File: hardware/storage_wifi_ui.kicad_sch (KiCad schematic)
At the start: 28 parts, among them J16 Keyboard KIN0-7 / KOUT0-7, J17 Keyboard power/reference, J18 I2C0, J19 Full-size SD, SPI, J20 ESP-01/ESP-01S socket, SW2 ESP_PROG, U34 AMS1117-3.3

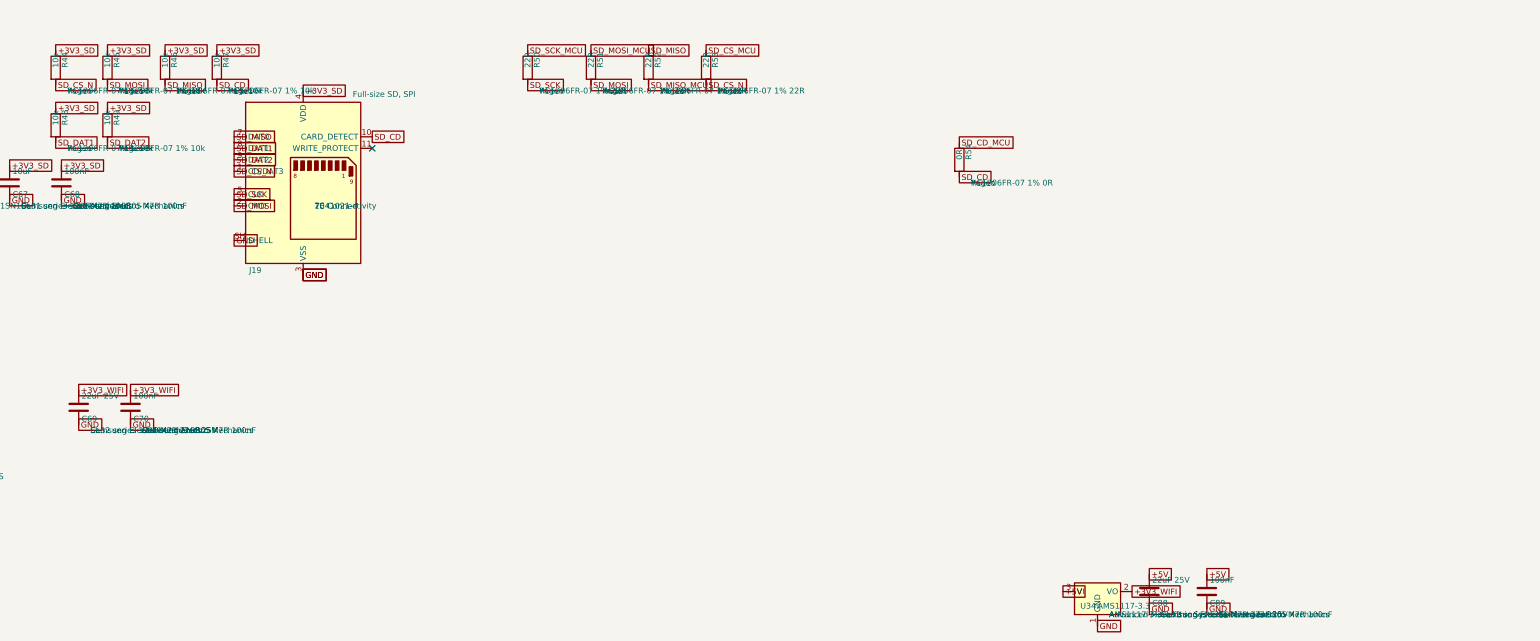
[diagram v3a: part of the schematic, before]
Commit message: Standardize passives and add microSD alternate
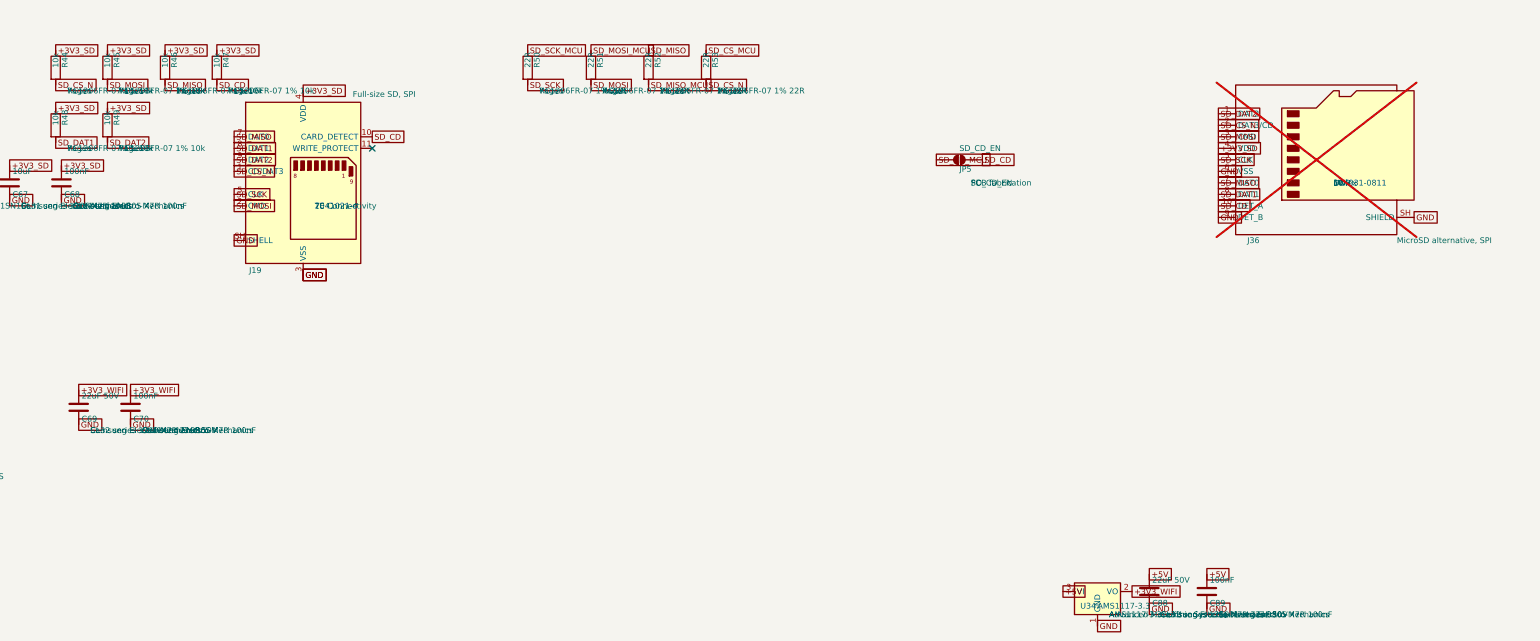
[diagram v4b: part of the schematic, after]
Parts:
- removed R54: 0R, Resistor_SMD:R_1206_3216Metric, symbol Device:R
- added J36: MicroSD alternative, SPI, Connector_Card:microSD_HC_Molex_104031-0811, symbol Connector:Micro_SD_Card_Det2
- added JP5: SD_CD_EN, LeanCam:SolderJumper_2_Open_1206Gap, symbol Jumper:SolderJumper_2_Open
- C69, C88: value 22uF 25V -> 22uF 50V; MPN CL32 series 1210 X7R 22uF 25V -> CL32 series 1210 X7R 22uF 50V
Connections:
- net +3V3_SD: now also J36.4 (VDD)
- net GND: now also J36.6 (VSS), J36.9 (DET_B), J36.SH (SHIELD)
- net SD_CD: now also J36.10 (DET_A), JP5.2 (B)
- net SD_CD_MCU: now also JP5.1 (A)
- net SD_CS_N: now also J36.2 (DAT3/CD)
- net SD_DAT1: now also J36.8 (DAT1)
- net SD_DAT2: now also J36.1 (DAT2)
- net SD_MISO: now also J36.7 (DAT0)
- net SD_MOSI: now also J36.3 (CMD)
- net SD_SCK: now also J36.5 (CLK)

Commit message: BOM simplification
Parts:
- C67: value 10uF -> 10uF 25V; MPN CL31 series 1206 X7R 10uF -> CL31 series 1206 X7R 10uF 25V
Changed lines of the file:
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@@
 		(instances
 			(project "Storage, Wi-Fi and UI"
-				(path "/9f4f8ddb-6d75-424f-85af-50d3b0c33d12"
+				(path "/ebd1e8ca-9dff-4053-89c8-43c30a776960"
 					(reference "J16")
 					(unit 1)
@@
 		(instances
 			(project "Storage, Wi-Fi and UI"
-				(path "/9f4f8ddb-6d75-424f-85af-50d3b0c33d12"
+				(path "/ebd1e8ca-9dff-4053-89c8-43c30a776960"
 					(reference "J17")
 					(unit 1)
@@
 		(instances
 			(project "Storage, Wi-Fi and UI"
-				(path "/9f4f8ddb-6d75-424f-85af-50d3b0c33d12"
+				(path "/ebd1e8ca-9dff-4053-89c8-43c30a776960"
 					(reference "RN22")
 					(unit 1)
@@
 		(instances
 			(project "Storage, Wi-Fi and UI"
-				(path "/9f4f8ddb-6d75-424f-85af-50d3b0c33d12"
+				(path "/ebd1e8ca-9dff-4053-89c8-43c30a776960"
 					(reference "RN24")
 					(unit 1)
@@
 		(instances
 			(project "Storage, Wi-Fi and UI"
-				(path "/9f4f8ddb-6d75-424f-85af-50d3b0c33d12"
+				(path "/ebd1e8ca-9dff-4053-89c8-43c30a776960"
 					(reference "J18")
 					(unit 1)
@@
 		(instances
 			(project "Storage, Wi-Fi and UI"
-				(path "/9f4f8ddb-6d75-424f-85af-50d3b0c33d12"
+				(path "/ebd1e8ca-9dff-4053-89c8-43c30a776960"
 					(reference "J19")
 					(unit 1)
@@
 		(instances
 			(project "Storage, Wi-Fi and UI"
-				(path "/9f4f8ddb-6d75-424f-85af-50d3b0c33d12"
+				(path "/ebd1e8ca-9dff-4053-89c8-43c30a776960"
 					(reference "R44")
 					(unit 1)
@@
 		(instances
 			(project "Storage, Wi-Fi and UI"
-				(path "/9f4f8ddb-6d75-424f-85af-50d3b0c33d12"
+				(path "/ebd1e8ca-9dff-4053-89c8-43c30a776960"
 					(reference "R45")
 					(unit 1)
@@
 		(instances
 			(project "Storage, Wi-Fi and UI"
-				(path "/9f4f8ddb-6d75-424f-85af-50d3b0c33d12"
+				(path "/ebd1e8ca-9dff-4053-89c8-43c30a776960"
 					(reference "R46")
 					(unit 1)
@@
 		(instances
 			(project "Storage, Wi-Fi and UI"
-				(path "/9f4f8ddb-6d75-424f-85af-50d3b0c33d12"
+				(path "/ebd1e8ca-9dff-4053-89c8-43c30a776960"
 					(reference "R47")
 					(unit 1)
@@
 		(instances
 			(project "Storage, Wi-Fi and UI"
-				(path "/9f4f8ddb-6d75-424f-85af-50d3b0c33d12"
+				(path "/ebd1e8ca-9dff-4053-89c8-43c30a776960"
 					(reference "R48")
 					(unit 1)
@@
 		(instances
 			(project "Storage, Wi-Fi and UI"
-				(path "/9f4f8ddb-6d75-424f-85af-50d3b0c33d12"
+				(path "/ebd1e8ca-9dff-4053-89c8-43c30a776960"
 					(reference "R49")
 					(unit 1)
@@
 		(instances
 			(project "Storage, Wi-Fi and UI"
-				(path "/9f4f8ddb-6d75-424f-85af-50d3b0c33d12"
+				(path "/ebd1e8ca-9dff-4053-89c8-43c30a776960"
 					(reference "R50")
 					(unit 1)
@@
 		(instances
 			(project "Storage, Wi-Fi and UI"
-				(path "/9f4f8ddb-6d75-424f-85af-50d3b0c33d12"
+				(path "/ebd1e8ca-9dff-4053-89c8-43c30a776960"
 					(reference "R51")
 					(unit 1)
@@
 		(instances
 			(project "Storage, Wi-Fi and UI"
-				(path "/9f4f8ddb-6d75-424f-85af-50d3b0c33d12"
+				(path "/ebd1e8ca-9dff-4053-89c8-43c30a776960"
 					(reference "R52")
 					(unit 1)
@@
 		(instances
 			(project "Storage, Wi-Fi and UI"
-				(path "/9f4f8ddb-6d75-424f-85af-50d3b0c33d12"
+				(path "/ebd1e8ca-9dff-4053-89c8-43c30a776960"
 					(reference "R53")
 					(unit 1)
@@
 		(instances
 			(project "Storage, Wi-Fi and UI"
-				(path "/9f4f8ddb-6d75-424f-85af-50d3b0c33d12"
+				(path "/ebd1e8ca-9dff-4053-89c8-43c30a776960"
 					(reference "FB2")
 					(unit 1)
@@
 			)
 		)
-		(property "Value" "10uF"
+		(property "Value" "10uF 25V"
 			(at 90.805 167.64 0.0000)
 			(effects
@@
 			)
 		)
-		(property "MPN" "CL31 series 1206 X7R 10uF"
+		(property "MPN" "CL31 series 1206 X7R 10uF 25V"
 			(at 92.71 175.2599 0)
 			(effects
@@
 		(instances
 			(project "Storage, Wi-Fi and UI"
-				(path "/9f4f8ddb-6d75-424f-85af-50d3b0c33d12"
+				(path "/ebd1e8ca-9dff-4053-89c8-43c30a776960"
 					(reference "C67")
 					(unit 1)
@@
 		(instances
 			(project "Storage, Wi-Fi and UI"
-				(path "/9f4f8ddb-6d75-424f-85af-50d3b0c33d12"
+				(path "/ebd1e8ca-9dff-4053-89c8-43c30a776960"
 					(reference "C68")
 					(unit 1)
@@
 		(instances
 			(project "Storage, Wi-Fi and UI"
-				(path "/9f4f8ddb-6d75-424f-85af-50d3b0c33d12"
+				(path "/ebd1e8ca-9dff-4053-89c8-43c30a776960"
 					(reference "JP5")
 					(unit 1)
@@
 		(instances
 			(project "Storage, Wi-Fi and UI"
-				(path "/9f4f8ddb-6d75-424f-85af-50d3b0c33d12"
+				(path "/ebd1e8ca-9dff-4053-89c8-43c30a776960"
 					(reference "J20")
 					(unit 1)
@@
 		(instances
 			(project "Storage, Wi-Fi and UI"
-				(path "/9f4f8ddb-6d75-424f-85af-50d3b0c33d12"
+				(path "/ebd1e8ca-9dff-4053-89c8-43c30a776960"
 					(reference "SW2")
 					(unit 1)
@@
 		(instances
 			(project "Storage, Wi-Fi and UI"
-				(path "/9f4f8ddb-6d75-424f-85af-50d3b0c33d12"
+				(path "/ebd1e8ca-9dff-4053-89c8-43c30a776960"
 					(reference "C69")
 					(unit 1)
@@
 		(instances
 			(project "Storage, Wi-Fi and UI"
-				(path "/9f4f8ddb-6d75-424f-85af-50d3b0c33d12"
+				(path "/ebd1e8ca-9dff-4053-89c8-43c30a776960"
 					(reference "C70")
 					(unit 1)
@@
 		(instances
 			(project "Storage, Wi-Fi and UI"
-				(path "/9f4f8ddb-6d75-424f-85af-50d3b0c33d12"
+				(path "/ebd1e8ca-9dff-4053-89c8-43c30a776960"
 					(reference "U34")
 					(unit 1)
@@
 		(instances
 			(project "Storage, Wi-Fi and UI"
-				(path "/9f4f8ddb-6d75-424f-85af-50d3b0c33d12"
+				(path "/ebd1e8ca-9dff-4053-89c8-43c30a776960"
 					(reference "C88")
 					(unit 1)
@@
 		(instances
 			(project "Storage, Wi-Fi and UI"
-				(path "/9f4f8ddb-6d75-424f-85af-50d3b0c33d12"
+				(path "/ebd1e8ca-9dff-4053-89c8-43c30a776960"
 					(reference "C89")
 					(unit 1)
@@
 		(instances
 			(project "Storage, Wi-Fi and UI"
-				(path "/9f4f8ddb-6d75-424f-85af-50d3b0c33d12"
+				(path "/ebd1e8ca-9dff-4053-89c8-43c30a776960"
 					(reference "RN36")
 					(unit 1)
@@
 		(instances
 			(project "Storage, Wi-Fi and UI"
-				(path "/9f4f8ddb-6d75-424f-85af-50d3b0c33d12"
+				(path "/ebd1e8ca-9dff-4053-89c8-43c30a776960"
 					(reference "J36")
 					(unit 1)

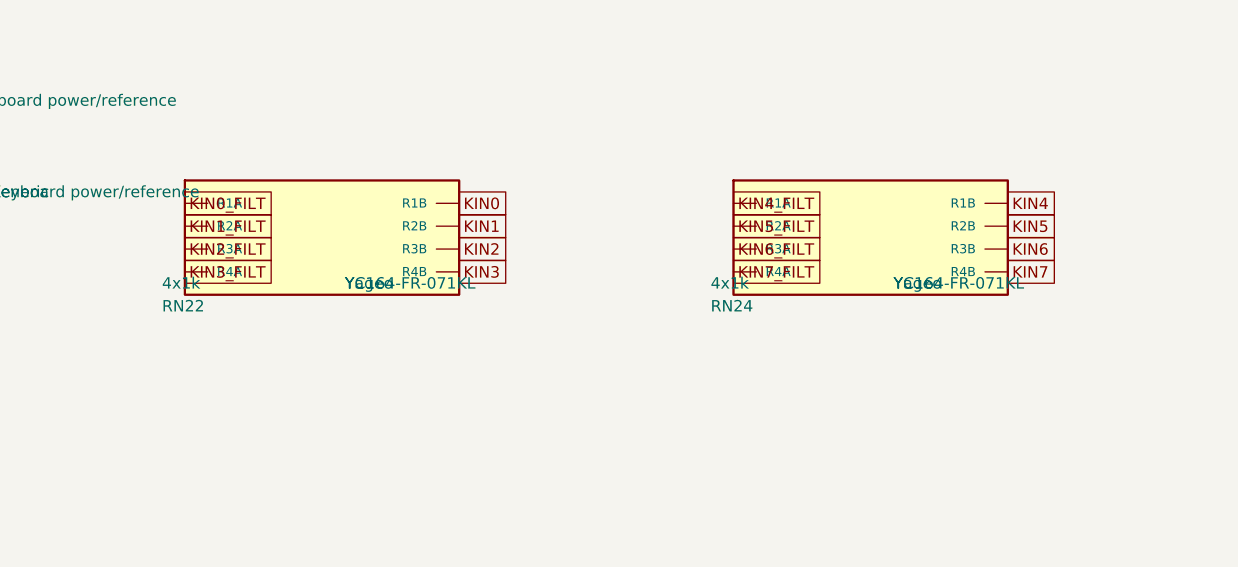
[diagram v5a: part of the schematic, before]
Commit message: Use 10k keyboard input networks
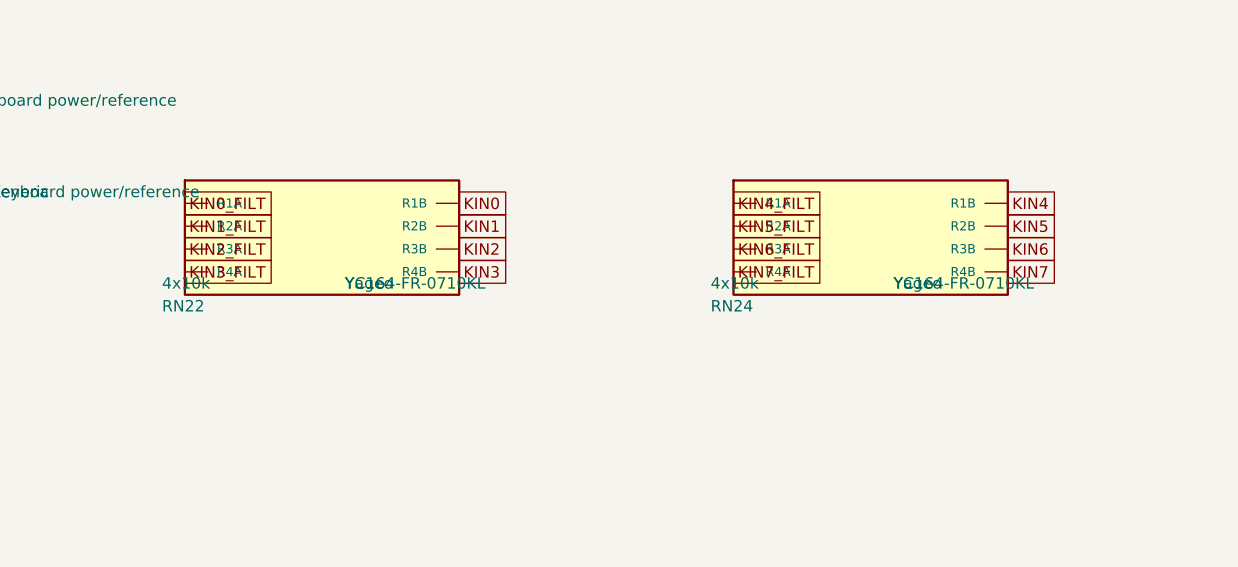
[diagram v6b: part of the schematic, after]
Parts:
- RN22, RN24: value 4x1k -> 4x10k; MPN YC164-FR-071KL -> YC164-FR-0710KL
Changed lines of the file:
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@@
 		(instances
 			(project "Storage, Wi-Fi and UI"
-				(path "/ebd1e8ca-9dff-4053-89c8-43c30a776960"
+				(path "/c5fb96bd-ffa6-4008-91b8-ee7edad8144e"
 					(reference "J16")
 					(unit 1)
@@
 		(instances
 			(project "Storage, Wi-Fi and UI"
-				(path "/ebd1e8ca-9dff-4053-89c8-43c30a776960"
+				(path "/c5fb96bd-ffa6-4008-91b8-ee7edad8144e"
 					(reference "J17")
 					(unit 1)
@@
 			)
 		)
-		(property "Value" "4x1k"
+		(property "Value" "4x10k"
 			(at 111.76 90.17 0.0000)
 			(effects
@@
 			)
 		)
-		(property "MPN" "YC164-FR-071KL"
+		(property "MPN" "YC164-FR-0710KL"
 			(at 132.08 90.1699 0)
 			(effects
@@
 		(instances
 			(project "Storage, Wi-Fi and UI"
-				(path "/ebd1e8ca-9dff-4053-89c8-43c30a776960"
+				(path "/c5fb96bd-ffa6-4008-91b8-ee7edad8144e"
 					(reference "RN22")
 					(unit 1)
@@
 			)
 		)
-		(property "Value" "4x1k"
+		(property "Value" "4x10k"
 			(at 172.72 90.17 0.0000)
 			(effects
@@
 			)
 		)
-		(property "MPN" "YC164-FR-071KL"
+		(property "MPN" "YC164-FR-0710KL"
 			(at 193.04 90.1699 0)
 			(effects
@@
 		(instances
 			(project "Storage, Wi-Fi and UI"
-				(path "/ebd1e8ca-9dff-4053-89c8-43c30a776960"
+				(path "/c5fb96bd-ffa6-4008-91b8-ee7edad8144e"
 					(reference "RN24")
 					(unit 1)
@@
 		(instances
 			(project "Storage, Wi-Fi and UI"
-				(path "/ebd1e8ca-9dff-4053-89c8-43c30a776960"
+				(path "/c5fb96bd-ffa6-4008-91b8-ee7edad8144e"
 					(reference "J18")
 					(unit 1)
@@
 		(instances
 			(project "Storage, Wi-Fi and UI"
-				(path "/ebd1e8ca-9dff-4053-89c8-43c30a776960"
+				(path "/c5fb96bd-ffa6-4008-91b8-ee7edad8144e"
 					(reference "J19")
 					(unit 1)
@@
 		(instances
 			(project "Storage, Wi-Fi and UI"
-				(path "/ebd1e8ca-9dff-4053-89c8-43c30a776960"
+				(path "/c5fb96bd-ffa6-4008-91b8-ee7edad8144e"
 					(reference "R44")
 					(unit 1)
@@
 		(instances
 			(project "Storage, Wi-Fi and UI"
-				(path "/ebd1e8ca-9dff-4053-89c8-43c30a776960"
+				(path "/c5fb96bd-ffa6-4008-91b8-ee7edad8144e"
 					(reference "R45")
 					(unit 1)
@@
 		(instances
 			(project "Storage, Wi-Fi and UI"
-				(path "/ebd1e8ca-9dff-4053-89c8-43c30a776960"
+				(path "/c5fb96bd-ffa6-4008-91b8-ee7edad8144e"
 					(reference "R46")
 					(unit 1)
@@
 		(instances
 			(project "Storage, Wi-Fi and UI"
-				(path "/ebd1e8ca-9dff-4053-89c8-43c30a776960"
+				(path "/c5fb96bd-ffa6-4008-91b8-ee7edad8144e"
 					(reference "R47")
 					(unit 1)
@@
 		(instances
 			(project "Storage, Wi-Fi and UI"
-				(path "/ebd1e8ca-9dff-4053-89c8-43c30a776960"
+				(path "/c5fb96bd-ffa6-4008-91b8-ee7edad8144e"
 					(reference "R48")
 					(unit 1)
@@
 		(instances
 			(project "Storage, Wi-Fi and UI"
-				(path "/ebd1e8ca-9dff-4053-89c8-43c30a776960"
+				(path "/c5fb96bd-ffa6-4008-91b8-ee7edad8144e"
 					(reference "R49")
 					(unit 1)
@@
 		(instances
 			(project "Storage, Wi-Fi and UI"
-				(path "/ebd1e8ca-9dff-4053-89c8-43c30a776960"
+				(path "/c5fb96bd-ffa6-4008-91b8-ee7edad8144e"
 					(reference "R50")
 					(unit 1)
@@
 		(instances
 			(project "Storage, Wi-Fi and UI"
-				(path "/ebd1e8ca-9dff-4053-89c8-43c30a776960"
+				(path "/c5fb96bd-ffa6-4008-91b8-ee7edad8144e"
 					(reference "R51")
 					(unit 1)
@@
 		(instances
 			(project "Storage, Wi-Fi and UI"
-				(path "/ebd1e8ca-9dff-4053-89c8-43c30a776960"
+				(path "/c5fb96bd-ffa6-4008-91b8-ee7edad8144e"
 					(reference "R52")
 					(unit 1)
@@
 		(instances
 			(project "Storage, Wi-Fi and UI"
-				(path "/ebd1e8ca-9dff-4053-89c8-43c30a776960"
+				(path "/c5fb96bd-ffa6-4008-91b8-ee7edad8144e"
 					(reference "R53")
 					(unit 1)
@@
 		(instances
 			(project "Storage, Wi-Fi and UI"
-				(path "/ebd1e8ca-9dff-4053-89c8-43c30a776960"
+				(path "/c5fb96bd-ffa6-4008-91b8-ee7edad8144e"
 					(reference "FB2")
 					(unit 1)
@@
 		(instances
 			(project "Storage, Wi-Fi and UI"
-				(path "/ebd1e8ca-9dff-4053-89c8-43c30a776960"
+				(path "/c5fb96bd-ffa6-4008-91b8-ee7edad8144e"
 					(reference "C67")
 					(unit 1)
@@
 		(instances
 			(project "Storage, Wi-Fi and UI"
-				(path "/ebd1e8ca-9dff-4053-89c8-43c30a776960"
+				(path "/c5fb96bd-ffa6-4008-91b8-ee7edad8144e"
 					(reference "C68")
 					(unit 1)
@@
 		(instances
 			(project "Storage, Wi-Fi and UI"
-				(path "/ebd1e8ca-9dff-4053-89c8-43c30a776960"
+				(path "/c5fb96bd-ffa6-4008-91b8-ee7edad8144e"
 					(reference "JP5")
 					(unit 1)
@@
 		(instances
 			(project "Storage, Wi-Fi and UI"
-				(path "/ebd1e8ca-9dff-4053-89c8-43c30a776960"
+				(path "/c5fb96bd-ffa6-4008-91b8-ee7edad8144e"
 					(reference "J20")
 					(unit 1)
@@
 		(instances
 			(project "Storage, Wi-Fi and UI"
-				(path "/ebd1e8ca-9dff-4053-89c8-43c30a776960"
+				(path "/c5fb96bd-ffa6-4008-91b8-ee7edad8144e"
 					(reference "SW2")
 					(unit 1)
@@
 		(instances
 			(project "Storage, Wi-Fi and UI"
-				(path "/ebd1e8ca-9dff-4053-89c8-43c30a776960"
+				(path "/c5fb96bd-ffa6-4008-91b8-ee7edad8144e"
 					(reference "C69")
 					(unit 1)
@@
 		(instances
 			(project "Storage, Wi-Fi and UI"
-				(path "/ebd1e8ca-9dff-4053-89c8-43c30a776960"
+				(path "/c5fb96bd-ffa6-4008-91b8-ee7edad8144e"
 					(reference "C70")
 					(unit 1)
@@
 		(instances
 			(project "Storage, Wi-Fi and UI"
-				(path "/ebd1e8ca-9dff-4053-89c8-43c30a776960"
+				(path "/c5fb96bd-ffa6-4008-91b8-ee7edad8144e"
 					(reference "U34")
 					(unit 1)
@@
 		(instances
 			(project "Storage, Wi-Fi and UI"
-				(path "/ebd1e8ca-9dff-4053-89c8-43c30a776960"
+				(path "/c5fb96bd-ffa6-4008-91b8-ee7edad8144e"
 					(reference "C88")
 					(unit 1)
@@
 		(instances
 			(project "Storage, Wi-Fi and UI"
-				(path "/ebd1e8ca-9dff-4053-89c8-43c30a776960"
+				(path "/c5fb96bd-ffa6-4008-91b8-ee7edad8144e"
 					(reference "C89")
 					(unit 1)
@@
 		(instances
 			(project "Storage, Wi-Fi and UI"
-				(path "/ebd1e8ca-9dff-4053-89c8-43c30a776960"
+				(path "/c5fb96bd-ffa6-4008-91b8-ee7edad8144e"
 					(reference "RN36")
 					(unit 1)
@@
 		(instances
 			(project "Storage, Wi-Fi and UI"
-				(path "/ebd1e8ca-9dff-4053-89c8-43c30a776960"
+				(path "/c5fb96bd-ffa6-4008-91b8-ee7edad8144e"
 					(reference "J36")
 					(unit 1)
